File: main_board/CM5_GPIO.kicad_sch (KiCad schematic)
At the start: 30 parts, among them IC4 TS921ID, IC6 TS921ID, J8 AudioJack3

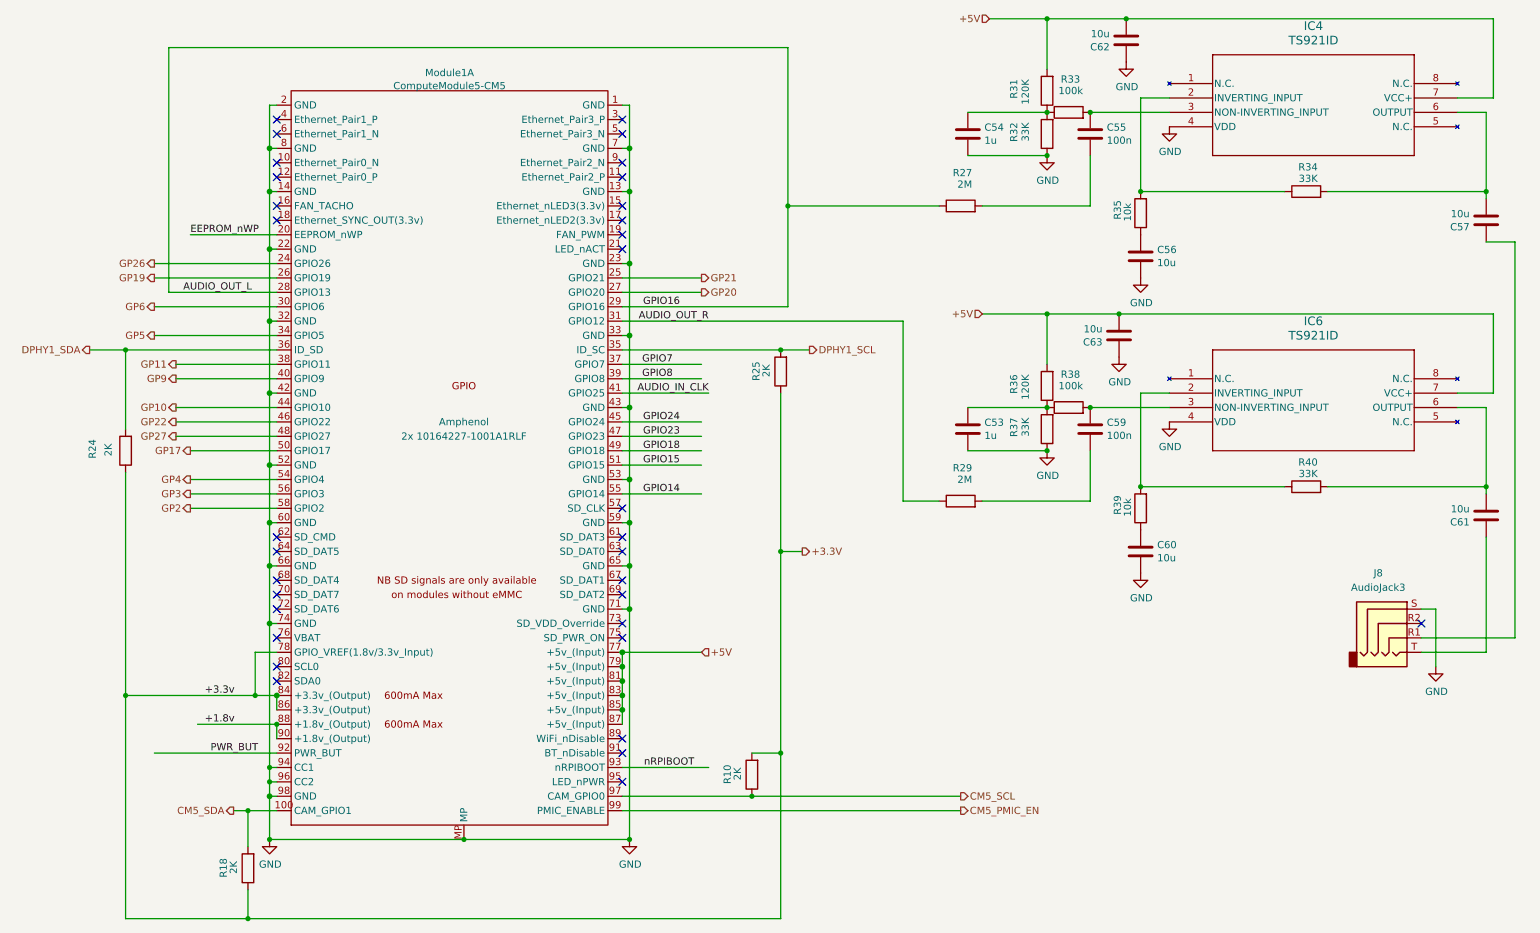
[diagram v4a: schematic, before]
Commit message: Use I2S sound chip instead of PWM output
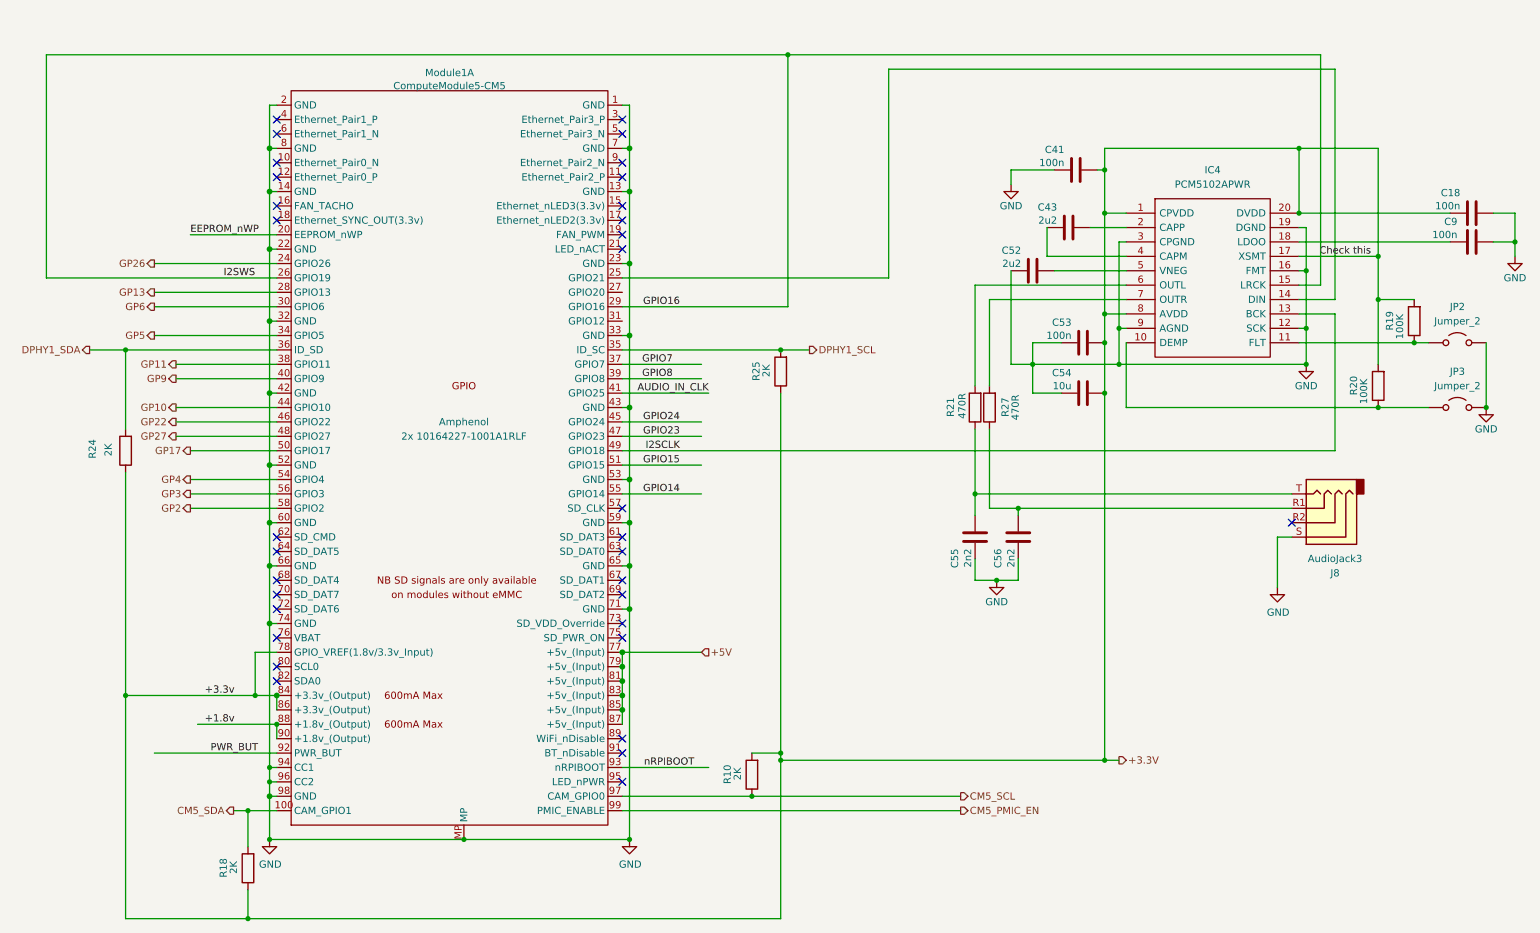
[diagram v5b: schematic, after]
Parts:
- removed C57, C60, C61, C62, C63: 10u, Capacitor_SMD:C_0805_2012Metric_Pad1.18x1.45mm_HandSolder, symbol Device:C
- removed C59: 100n, Capacitor_SMD:C_0805_2012Metric_Pad1.18x1.45mm_HandSolder, symbol Device:C
- removed IC4, IC6: TS921ID, 000_custom:S0-8_3P9X4P9_STM, symbol 000_Custom:TS921ID
- removed R29: 2M, Resistor_SMD:R_0805_2012Metric_Pad1.20x1.40mm_HandSolder, symbol Device:R
- removed R31, R36: 120K, Resistor_SMD:R_0805_2012Metric_Pad1.20x1.40mm_HandSolder, symbol Device:R
- removed R32, R34, R37, R40: 33K, Resistor_SMD:R_0805_2012Metric_Pad1.20x1.40mm_HandSolder, symbol Device:R
- removed R33, R38: 100k, Resistor_SMD:R_0805_2012Metric_Pad1.20x1.40mm_HandSolder, symbol Device:R
- removed R35, R39: 10k, Resistor_SMD:R_0805_2012Metric_Pad1.20x1.40mm_HandSolder, symbol Device:R
- added C18, C41, C9: 100n, Capacitor_SMD:C_0805_2012Metric_Pad1.18x1.45mm_HandSolder, symbol Device:C
- added C43, C52: 2u2, Capacitor_SMD:C_0805_2012Metric_Pad1.18x1.45mm_HandSolder, symbol Device:C
- added IC4: PCM5102APWR, 000_custom:SOP65P640X120-20N, symbol 000_Custom:PCM5102APWR
- added JP2, JP3: Jumper_2, Jumper:SolderJumper-2_P1.3mm_Bridged2Bar_RoundedPad1.0x1.5mm, symbol Jumper:Jumper_2_Open
- added R19, R20: 100K, Resistor_SMD:R_0805_2012Metric_Pad1.20x1.40mm_HandSolder, symbol Device:R
- added R21: 470R, Resistor_SMD:R_0805_2012Metric_Pad1.20x1.40mm_HandSolder, symbol Device:R
- C53: value 1u -> 100n; Field4 Farnell -> Digikey; Field5 2611911 -> 490-14381-1-ND; Field6 RM EMK105 B7104KV-F -> GRM21BR71A106KA73L; Field7 TAIYO YUDEN EUROPE GMBH -> Murata; Field8 110091611 -> 111893011; Part Description 0.1uF 10% 16V Ceramic Capacitor X7R 0402 (1005 Metric) -> 10uF 10% 10V Ceramic Capacitor X7R 0805 (2012 Metric)
- C54: value 1u -> 10u; Field4 Farnell -> Digikey; Field5 2611911 -> 490-14381-1-ND; Field6 RM EMK105 B7104KV-F -> GRM21BR71A106KA73L; Field7 TAIYO YUDEN EUROPE GMBH -> Murata; Field8 110091611 -> 111893011; Part Description 0.1uF 10% 16V Ceramic Capacitor X7R 0402 (1005 Metric) -> 10uF 10% 10V Ceramic Capacitor X7R 0805 (2012 Metric)
- C55: value 100n -> 2n2; Field4 Farnell -> Digikey; Field5 2611911 -> 490-14381-1-ND; Field6 RM EMK105 B7104KV-F -> GRM21BR71A106KA73L; Field7 TAIYO YUDEN EUROPE GMBH -> Murata; Field8 110091611 -> 111893011; Part Description 0.1uF 10% 16V Ceramic Capacitor X7R 0402 (1005 Metric) -> 10uF 10% 10V Ceramic Capacitor X7R 0805 (2012 Metric)
- C56: value 10u -> 2n2; Field4 Farnell -> Digikey; Field5 2611911 -> 490-14381-1-ND; Field6 RM EMK105 B7104KV-F -> GRM21BR71A106KA73L; Field7 TAIYO YUDEN EUROPE GMBH -> Murata; Field8 110091611 -> 111893011; Part Description 0.1uF 10% 16V Ceramic Capacitor X7R 0402 (1005 Metric) -> 10uF 10% 10V Ceramic Capacitor X7R 0805 (2012 Metric)
- R27: value 2M -> 470R
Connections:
- net +3.3V: now also C53.2, C54.2, C18.1, C41.2, IC4.1 (CPVDD), IC4.17 (XSMT), IC4.20 (DVDD), IC4.8 (AVDD), R19.2, R20.2
- net GND: now also C53.1, C54.1, C55.1, C56.1, C18.2, C41.1, C52.1, C9.2, IC4.12 (SCK), IC4.16 (FMT), IC4.19 (DGND), IC4.3 (CPGND), IC4.9 (AGND), JP2.2 (B), JP3.2 (B); no longer C53.2, C54.2, C56.2
- net at J8.T: now also C55.2, R21.1
- net at R27.2: now also IC4.7 (OUTR); no longer C55.2
- net at J8.R1: now also C56.2, R27.1
- removed net AUDIO_OUT_L: Module1.28 (GPIO13), Module1.29 (GPIO16), R27.1
- net AUDIO_OUT_R: no longer names the net of Module1.31 (GPIO12)
- net GP19 renamed GPIO16
- net GPIO16: now also Module1.29 (GPIO16), IC4.15 (LRCK)
- net GP20: no longer names the net of Module1.27 (GPIO20)
- net GP21: no longer names the net of Module1.25 (GPIO21)
- net GP21: now also IC4.14 (DIN)
- net GPIO18 renamed I2SCLK
- net I2SCLK: now also IC4.13 (BCK)
- new net: IC4.11 (FLT), JP2.1 (A), R19.1
- new net: IC4.6 (OUTL), R21.2
- new net: C9.1, IC4.18 (LDOO)
- new net: IC4.10 (DEMP), JP3.1 (A), R20.1
- new net: C43.2, IC4.2 (CAPP)
- new net: C43.1, IC4.4 (CAPM)
- new net: C52.2, IC4.5 (VNEG)
- new net GP13: Module1.28 (GPIO13)
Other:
- moved on the sheet: J8

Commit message: Minor fixes
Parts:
- removed JP3: Jumper_2, Jumper:SolderJumper-2_P1.3mm_Bridged2Bar_RoundedPad1.0x1.5mm, symbol Jumper:Jumper_2_Open
- removed R20: 100K, Resistor_SMD:R_0805_2012Metric_Pad1.20x1.40mm_HandSolder, symbol Device:R
- JP2: footprint Jumper:SolderJumper-2_P1.3mm_Bridged2Bar_RoundedPad1.0x1.5mm -> Jumper:SolderJumper-2_P1.3mm_Open_RoundedPad1.0x1.5mm
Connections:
- net GND: now also IC4.10 (DEMP)
